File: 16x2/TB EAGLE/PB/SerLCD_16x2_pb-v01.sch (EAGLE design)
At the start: 19 parts, among them J1 AVR_PROG, J3 SER_LCD16X2, U1 5V Flying Jalapeno, U2 74LVC4066_MUX_1:1_X4

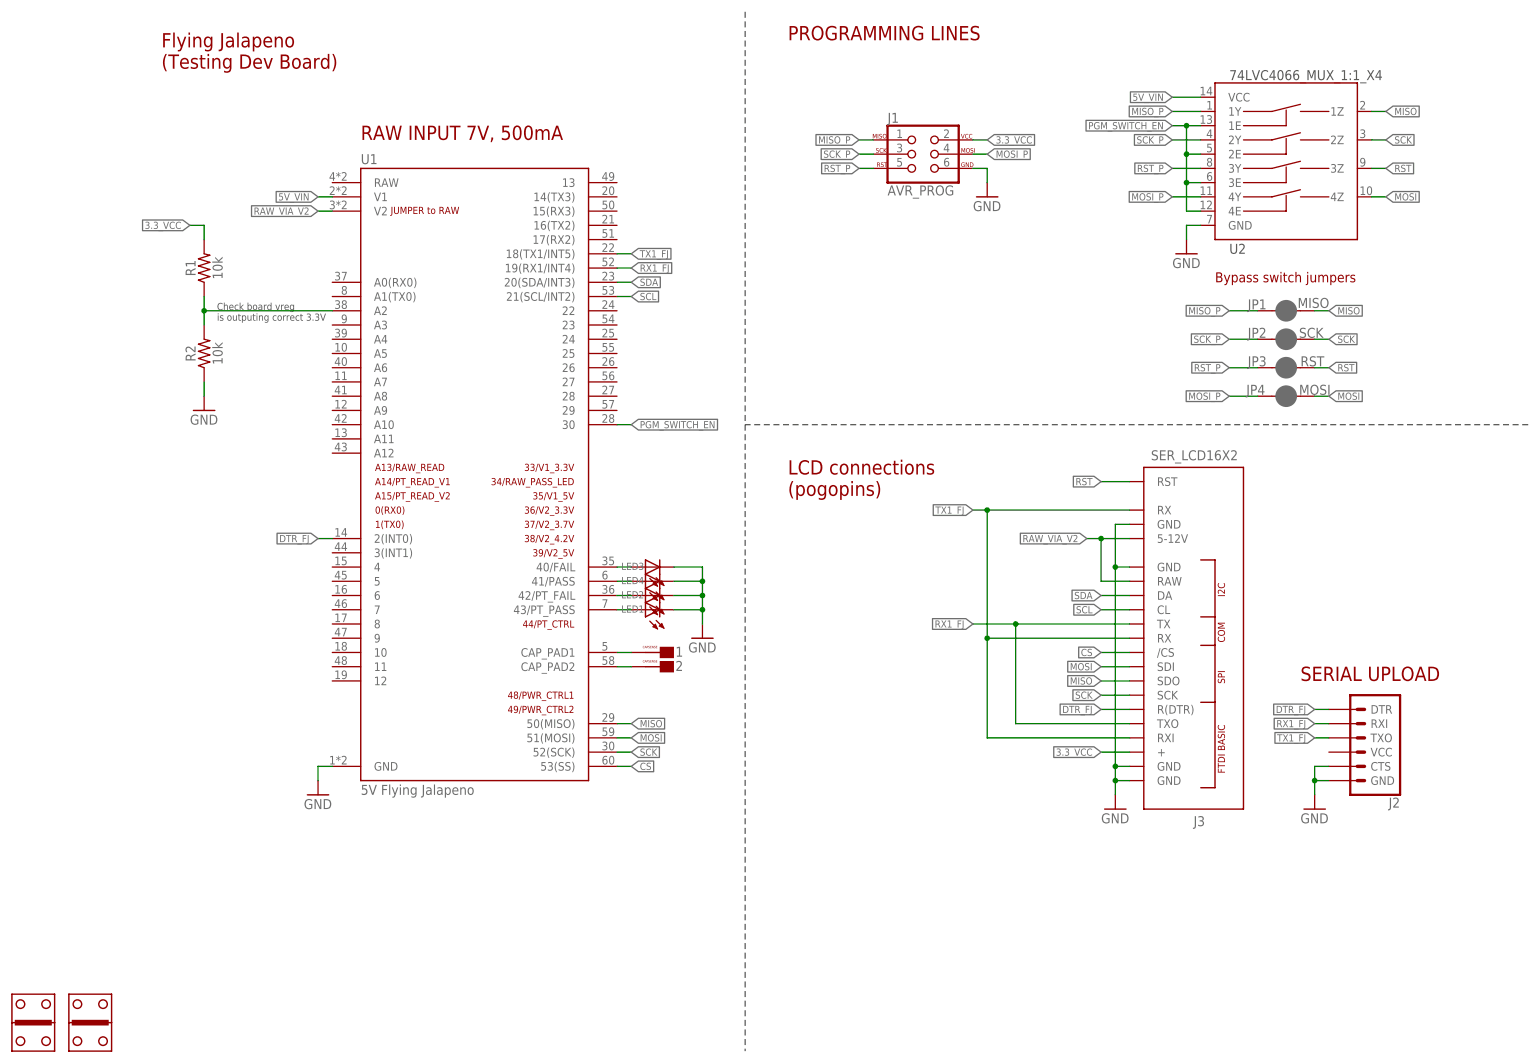
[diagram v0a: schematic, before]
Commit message: added preTest to 3.3V on 16x2
This will also be used to verify that the vreg is outputing proper
voltage later in the test.

NOTE: I still need to add this to 20x4 version
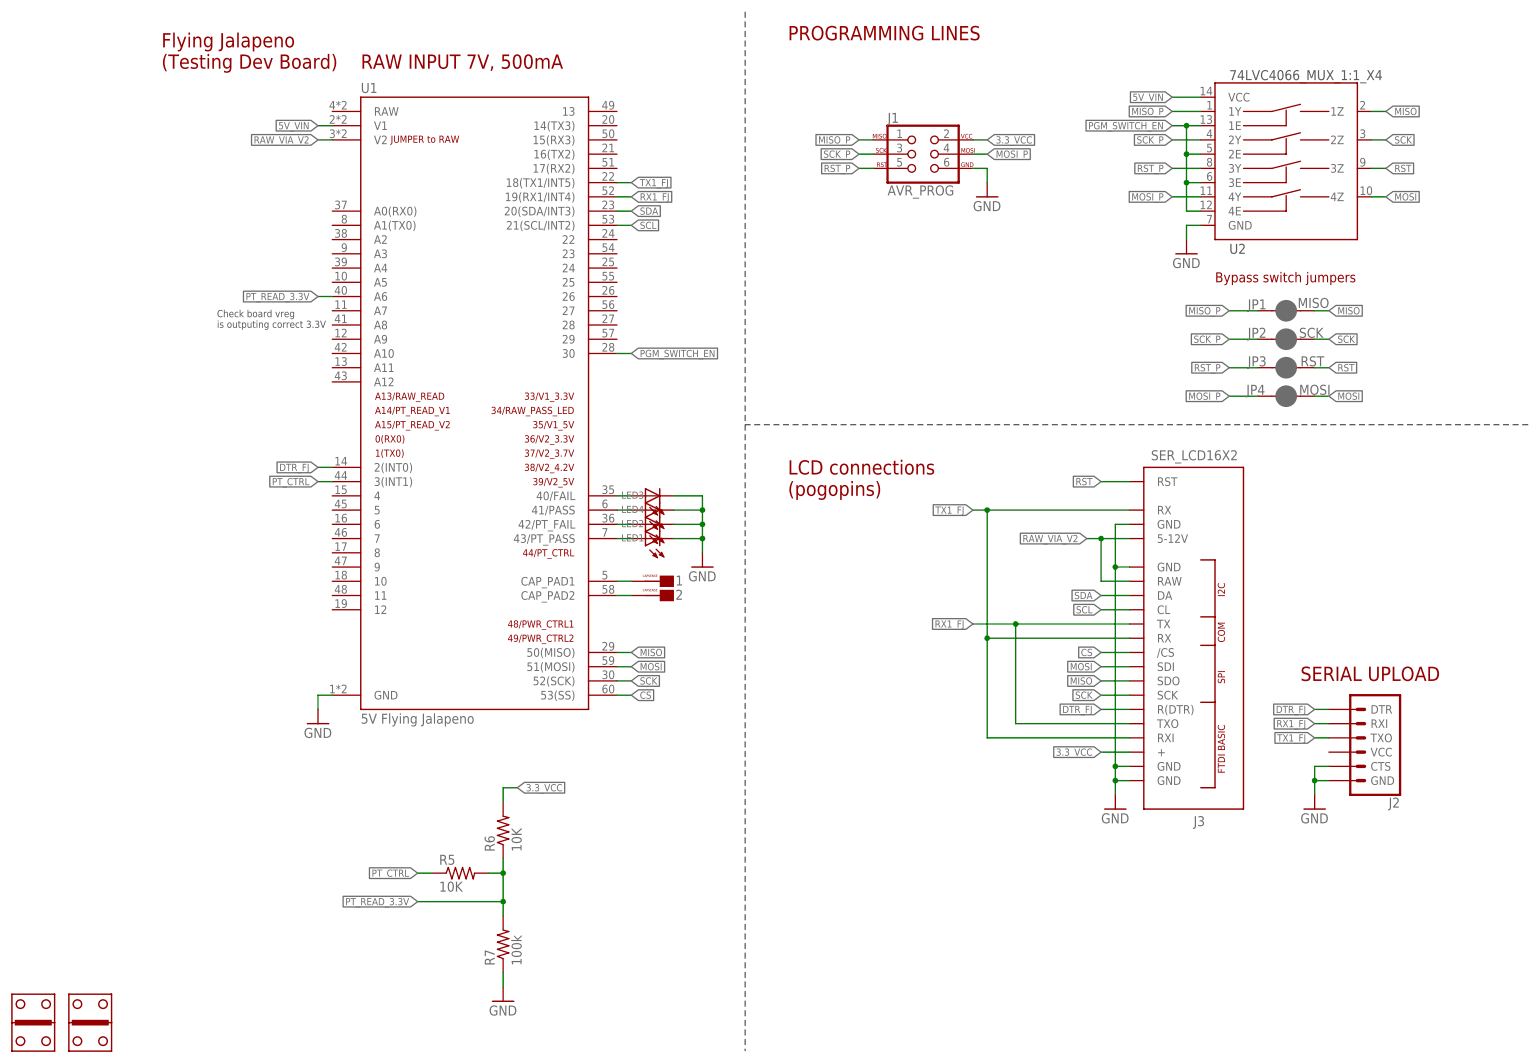
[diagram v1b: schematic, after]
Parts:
- removed R1, R2: 10k, SparkFun-Resistors:10KOHM-0603-1/10W-1%
- added R5, R6: 10K, SparkFun-Resistors:10KOHM1/10W1%(0603)0603
- added R7: 100k, SparkFun-Resistors:100KOHM1/10W1%(0603)
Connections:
- removed net N$7: R1.1, R2.2, U1.A2
- new net PT_CTRL: R5.1, U1.3(INT1)
- new net PT_READ_3.3V: R5.2, R6.1, R7.2, U1.A6
- net 3.3_VCC: now also R6.2; no longer R1.2
- net GND: now also R7.1; no longer R2.1
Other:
- moved on the sheet: 1, 2, LED1, LED2, LED3, LED4, U1

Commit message: updating switch circuit and re-routing
the pi_grammer has the isolation switch, so I am now using the onboard switch to isolate the FJ's SPI lines. This will hopefully elliminate the need for the occasional hard reset on the testbed.

Re-routing everything manually. The original design was autorouted and was pretty ugly.

Currently most of the important stuff is routed nicely. Still needs LEDs and some switch stuff routed.
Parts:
- removed JP1: MISO, SparkFun-Jumpers:JUMPER-SMT_2_NC_PASTE_NO-SILK
- removed JP2: SCK, SparkFun-Jumpers:JUMPER-SMT_2_NC_PASTE_NO-SILK
- removed JP3: RST, SparkFun-Jumpers:JUMPER-SMT_2_NC_PASTE_NO-SILK
- removed JP4: MOSI, SparkFun-Jumpers:JUMPER-SMT_2_NC_PASTE_NO-SILK
- added C1: (no value), Testing:CAP0603-CAP
- U1: device Testing:FLYING_JALAPENO_V2MALE -> Testing:FLYING_JALAPENO_V3MALE
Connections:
- net PGM_SWITCH_EN renamed SPI_SWITCH_EN
- removed net MISO_P: J1.1, JP1.1, U2.1Y
- removed net MOSI_P: J1.4, JP4.1, U2.4Y
- removed net RST_P: J1.5, JP3.1, U2.3Y
- removed net SCK_P: J1.3, JP2.1, U2.2Y
- new net CS_FJ: U1.53(SS), U2.3Z
- new net MISO_FJ: U1.50(MISO), U2.1Z
- new net MOSI_FJ: U1.51(MOSI), U2.4Z
- new net SCK_FJ: U1.52(SCK), U2.2Z
- net 5V_VIN: now also C1.1
- net CS: now also U2.3Y; no longer U1.53(SS)
- net GND: now also C1.2
- net MISO: now also J1.1, U2.1Y; no longer JP1.2, U1.50(MISO), U2.1Z
- net MOSI: now also J1.4, U2.4Y; no longer JP4.2, U1.51(MOSI), U2.4Z
- net RST: now also J1.5; no longer JP3.2, U2.3Z
- net RX1_FJ: no longer J3.TXO
- net SCK: now also J1.3, U2.2Y; no longer JP2.2, U1.52(SCK), U2.2Z
- net TX1_FJ: no longer J3.RX@19, J3.RXI
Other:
- note added: "PROGRAMMING LINES / SPI Switch"
- note removed: "Bypass switch jumpers"
- note removed: "PROGRAMMING LINES"
- moved on the sheet: J1
